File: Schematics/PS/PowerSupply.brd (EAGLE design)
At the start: 99.1 x 76.2 mm, 38 parts, among them T1 IRFP240, T2 IRFP240

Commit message: PS schem updates
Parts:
- added C10, C7, C8, C9: 0.1uF, rcl:C102-064X133
- added C11, C12: 1uF, rcl:C102-064X133
- added C13, C19: 15,000uF, Amplifier_Parts:PHI-35
- added D10, D5, D8, D9: VS-ETL1506-M3, Amplifier_Parts:VS-ETL1506-M3
- added R12: 100, resistor:0207/15
- added R16: 2k, rcl:VTA52
- added R17, R18: 1, rcl:0411/12
- R2: value 100 -> 2k; device resistor:0207/15 -> rcl:VTA52
- R6: value 560 -> 330
- R7: value 390 -> 33; device rcl:0204V -> rcl:0309V
- moved R2 358.2 mm to (-114.0, -270.5), turned to 0 degrees
- moved R7 282.3 mm to (-127.5, -186.2), turned to 0 degrees
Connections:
- net N$24 renamed VAC+40
- net N$26 renamed VAC+15
- net N$27 renamed VAC-15
- net N$9 renamed VAC-40
- removed net N$25: TRAFO1.P$13
- removed net N$28: TRAFO1.P$18
- new net N$23: D5.P$4, D8.P$3
- new net N$24: D10.C, D9.A
- new net N$8: C9.2, R17.2
- new net N$9: D5.A, D8.C
- new net SGND: C10.1, C11.2, C12.1, C13.+, C19.-, C7.2, C8.1, R12.1, R16.2, R17.1, R2.1, TRAFO1.P$13, TRAFO1.P$18
- new net VEE: C12.2, C13.-, C8.2, D10.A, D8.A, R16.1, R18.1
- net GND: now also R12.2; no longer R2.1
- net N$10: now also R7.1; no longer R7.2
- net N$11: now also R7.2; no longer R7.1
- net N$3: now also C10.2, R18.2; no longer R2.2, U$3.P$3
- net VCC: now also C11.1, C19.+, C7.1, C9.1, D5.C, D9.C, R2.2
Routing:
- net N$10: track 36.1 -> 9.41 mm
- net N$3: track 12.4 -> 0.00 mm
- net N$11: track 23.7 -> 17.3 mm

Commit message: updates to PS
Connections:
- removed net N$24: D10.C, D9.A
- removed net N$9: D5.A, D8.C
- net VAC+40: now also D5.A, D8.C
- net VAC-40: now also D10.C, D9.A
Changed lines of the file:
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@@
 <contactref element="TRAFO1" pad="P$11"/>
 <contactref element="TRAFO1" pad="P$12"/>
+<contactref element="D5" pad="A"/>
+<contactref element="D8" pad="C"/>
 <wire x1="-120.904" y1="-124.206" x2="-125.984" y2="-124.206" width="0" layer="19" extent="1-1"/>
+<wire x1="-135.684" y1="-290.068" x2="-125.984" y2="-124.206" width="0" layer="19" extent="1-1"/>
+<wire x1="-158.194" y1="-290.068" x2="-135.684" y2="-290.068" width="0" layer="19" extent="1-1"/>
 </signal>
 <signal name="VAC-40">
 <contactref element="TRAFO1" pad="P$14"/>
 <contactref element="TRAFO1" pad="P$15"/>
+<contactref element="D9" pad="A"/>
+<contactref element="D10" pad="C"/>
 <wire x1="-105.664" y1="-124.206" x2="-110.744" y2="-124.206" width="0" layer="19" extent="1-1"/>
+<wire x1="-168.704" y1="-290.068" x2="-110.744" y2="-124.206" width="0" layer="19" extent="1-1"/>
+<wire x1="-191.214" y1="-290.068" x2="-168.704" y2="-290.068" width="0" layer="19" extent="1-1"/>
 </signal>
 <signal name="VAC+15">
@@
 <wire x1="-129.286" y1="-270.51" x2="-118.618" y2="-280.416" width="0" layer="19" extent="1-1"/>
 </signal>
-<signal name="N$9">
-<contactref element="D5" pad="A"/>
-<contactref element="D8" pad="C"/>
-<wire x1="-135.684" y1="-290.068" x2="-158.194" y2="-290.068" width="0" layer="19" extent="1-1"/>
-</signal>
-<signal name="N$24">
-<contactref element="D9" pad="A"/>
-<contactref element="D10" pad="C"/>
-<wire x1="-168.704" y1="-290.068" x2="-191.214" y2="-290.068" width="0" layer="19" extent="1-1"/>
-</signal>
 </signals>

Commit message: updates to PS schematic, created special 1N4004 part
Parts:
- added C14, C21, C22: 1uF, rcl:E2,5-6
- added C18, C20: 0.1uF, rcl:C102-064X133
- added C6: 10uF, rcl:C102-064X133
- added D11, D12, D13, D14, D15, D16: 1N4004, Amplifier_Parts:1N4004
- added IC1: LM317MABDT, v-reg:DPACK
- added R19, R20: 10k, rcl:0204V
- D1: device diode:DO41-10 -> Amplifier_Parts:1N4004
- moved TRAFO1 187.3 mm to (28.4, 49.8)
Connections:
- net N$12 renamed MUTE
- removed net N$3: C10.2, R18.2
- new net N$25: C10.1, R18.1
- new net N$26: C6.1, D12.A, IC1.1, R19.1, R20.2
- new net VCC1: C18.1, C21.+, D11.C, D13.C, D15.C, IC1.3
- new net VEE1: C20.2, C22.-, D14.A, D16.A
- net N$23: now also C14.+, D11.A, D12.C, IC1.4, R19.2; no longer D5.P$4, D8.P$3
- net SGND: now also C14.-, C18.2, C20.1, C21.-, C22.+, C6.2, R18.2, R20.1; no longer C10.1
- net VAC+15: now also D13.A, D14.C
- net VAC-15: now also D15.A, D16.C
- net VAC-40: now also D10.P$4
- net VCC: no longer U$3.P$2
- net VEE: now also C10.2; no longer R18.1
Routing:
- net N$10: track 9.41 -> 15.1 mm

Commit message: updates to PS, it is finished
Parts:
- added C16, C23, C25: 1uF, rcl:E2,5-6
- added C24: 10uF, resistor:C025-025X050
- added D17, D18: 1N4004, Amplifier_Parts:1N4004
- added IC2: LM337, Amplifier_Parts:LM337
- added R21, R22: 10k, rcl:0204V
- C1: device rcl:C050-035X075 -> resistor:C025-025X050
- C6: device rcl:C102-064X133 -> resistor:C025-025X050
- D6, D7: value 1N4933 -> 1N4004; device diode:DO41-10 -> Amplifier_Parts:1N4004
- U$3: value SCREW_TERMINAL_5 -> SCREW_TERMINAL_6; device Amplifier_Parts:SCREW_TERMINAL_5 -> Amplifier_Parts:SCREW_TERMINAL_6
- moved D6 362.0 mm to (-223.5, -449.6)
- moved D7 358.5 mm to (-225.0, -451.9)
- moved C14 128.6 mm to (-223.0, -456.2)
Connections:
- removed net N$23: C14.+, D11.A, D12.C, IC1.4, R19.2
- removed net VCC1: C18.1, C21.+, D11.C, D13.C, D15.C, IC1.3
- removed net VEE1: C20.2, C22.-, D14.A, D16.A
- new net N$3: C24.2, D17.C, IC2.1, R21.1, R22.2
- new net V-: C25.-
- new net V-15UN: C20.2, C22.-, C23.-, D14.A, D16.A, D18.A, IC2.4
- new net V15+: C14.+, D11.A, D12.C, IC1.4, R19.2, U$3.P$2
- new net V15-: D17.A, D18.C, IC2.3, R22.1, U$3.P$4
- new net V15UN: C16.+, C18.1, C21.+, D11.C, D13.C, D15.C, IC1.3
- net GND: now also U$2.P$5
- net MUTE: now also U$3.P$6
- net PE: no longer U$2.P$5
- net SGND: now also C16.-, C23.+, C24.1, C25.+, R21.2, U$3.P$3
- net VCC: now also U$3.P$1
- net VEE: now also U$3.P$5

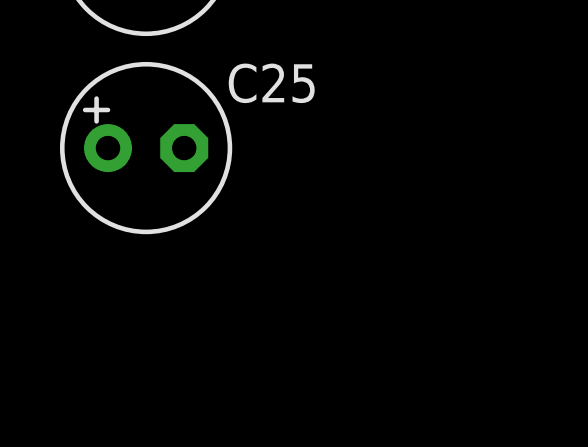
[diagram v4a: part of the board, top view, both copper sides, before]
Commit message: added DC blocking cap on trafo
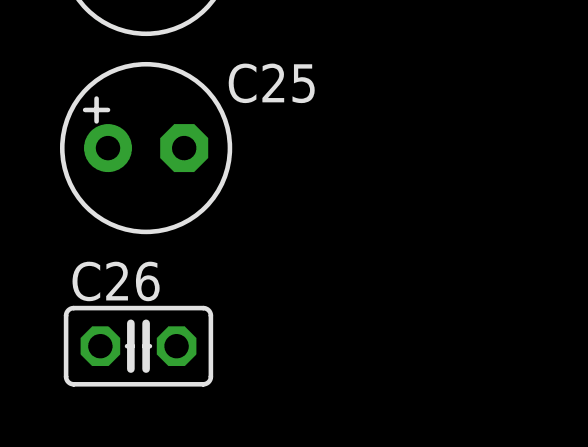
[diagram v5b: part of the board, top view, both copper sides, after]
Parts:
- added C26: 1uF, resistor:C025-025X050
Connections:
- new net N$9: C26.2, TRAFO1.P$10, TRAFO1.P$6, TRAFO1.P$7, TRAFO1.P$8, TRAFO1.P$9
- net GND: now also C26.1; no longer TRAFO1.P$10, TRAFO1.P$6, TRAFO1.P$7, TRAFO1.P$8, TRAFO1.P$9
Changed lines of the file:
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@@
 <element name="C14" library="rcl" package="E2,5-6" value="1uF" x="-223.012" y="-456.184"/>
 <element name="C25" library="rcl" package="E2,5-6" value="1uF" x="-223.012" y="-462.788"/>
+<element name="C26" library="resistor" package="C025-025X050" value="1uF" x="-223.266" y="-469.392"/>
 </elements>
 <signals>
@@
 <contactref element="U$1" pad="COIL+"/>
 <contactref element="U$6" pad="V-"/>
-<contactref element="TRAFO1" pad="P$7"/>
-<contactref element="TRAFO1" pad="P$6"/>
-<contactref element="TRAFO1" pad="P$8"/>
-<contactref element="TRAFO1" pad="P$9"/>
-<contactref element="TRAFO1" pad="P$10"/>
 <contactref element="U$5" pad="4"/>
 <contactref element="C1" pad="1"/>
@@
 <contactref element="R12" pad="2"/>
 <contactref element="U$2" pad="P$5"/>
-<wire x1="-117.602" y1="-141.224" x2="-61.976" y2="-105.791" width="0" layer="19" extent="1-1"/>
-<wire x1="-127.254" y1="-153.416" x2="-117.602" y2="-141.224" width="0" layer="19" extent="1-1"/>
-<wire x1="-127.254" y1="-159.766" x2="-127.254" y2="-153.416" width="0" layer="19" extent="1-1"/>
-<wire x1="-114.046" y1="-192.024" x2="-127.254" y2="-159.766" width="0" layer="19" extent="1-1"/>
+<contactref element="C26" pad="1"/>
+<wire x1="-114.046" y1="-192.024" x2="-224.536" y2="-469.392" width="0" layer="19" extent="1-1"/>
+<wire x1="-127.254" y1="-159.766" x2="-114.046" y2="-192.024" width="0" layer="19" extent="1-1"/>
+<wire x1="-127.254" y1="-153.416" x2="-127.254" y2="-159.766" width="0" layer="19" extent="1-1"/>
+<wire x1="-117.602" y1="-141.224" x2="-127.254" y2="-153.416" width="0" layer="19" extent="1-1"/>
+<wire x1="-61.976" y1="-105.791" x2="-117.602" y2="-141.224" width="0" layer="19" extent="1-1"/>
 <wire x1="1.864" y1="-71.572" x2="-61.976" y2="-105.791" width="0" layer="19" extent="1-1"/>
 <wire x1="1.524" y1="-40.64" x2="1.864" y2="-71.572" width="0" layer="19" extent="1-1"/>
+<wire x1="10.668" y1="-35.306" x2="1.524" y2="-40.64" width="0" layer="19" extent="1-1"/>
 <wire x1="-9.286" y1="-42.578" x2="1.524" y2="-40.64" width="0" layer="19" extent="1-1"/>
-<wire x1="10.668" y1="-35.306" x2="1.524" y2="-40.64" width="0" layer="19" extent="1-1"/>
 <wire x1="30.48" y1="7.62" x2="10.668" y2="-35.306" width="0" layer="19" extent="16-16"/>
-<wire x1="30.988" y1="49.784" x2="25.287265625" y2="52.367478125" width="0" layer="19" extent="1-1"/>
-<wire x1="36.068" y1="49.784" x2="30.988" y2="49.784" width="0" layer="19" extent="1-1"/>
-<wire x1="41.148" y1="49.784" x2="36.068" y2="49.784" width="0" layer="19" extent="1-1"/>
-<wire x1="46.228" y1="49.784" x2="41.148" y2="49.784" width="0" layer="19" extent="1-1"/>
-<wire x1="51.308" y1="49.784" x2="46.228" y2="49.784" width="0" layer="19" extent="1-1"/>
-<wire x1="55.55415" y1="45.591403125" x2="51.308" y2="49.784" width="0" layer="19" extent="1-1"/>
-<wire x1="45.658725" y1="43.20528125" x2="46.228" y2="49.784" width="0" layer="19" extent="1-1"/>
+<wire x1="4.54" y1="29.16" x2="8.298521875" y2="37.41" width="0" layer="19" extent="16-16"/>
+<wire x1="44.892303125" y1="30.808921875" x2="48.702303125" y2="18.108921875" width="0" layer="19" extent="1-1"/>
+<wire x1="45.658725" y1="43.20528125" x2="44.892303125" y2="30.808921875" width="0" layer="19" extent="1-1"/>
+<wire x1="55.55415" y1="45.591403125" x2="45.658725" y2="43.20528125" width="0" layer="19" extent="1-1"/>
 <wire x1="59.567503125" y1="39.844834375" x2="55.55415" y2="45.591403125" width="0" layer="19" extent="1-1"/>
-<wire x1="4.54" y1="29.16" x2="8.298521875" y2="37.41" width="0" layer="19" extent="16-16"/>
 <wire x1="70.620678125" y1="34.528765625" x2="59.567503125" y2="39.844834375" width="0" layer="19" extent="1-1"/>
-<wire x1="44.892303125" y1="30.808921875" x2="45.658725" y2="43.20528125" width="0" layer="19" extent="1-1"/>
 <wire x1="56.795371875" y1="3.327840625" x2="48.37338125" y2="17.78" width="0" layer="19" extent="16-16"/>
 <wire x1="61.9296125" y1="3.109978125" x2="56.795371875" y2="3.327840625" width="0" layer="19" extent="1-1"/>
@@
 <contactref element="C25" pad="-"/>
 </signal>
+<signal name="N$9">
+<contactref element="TRAFO1" pad="P$6"/>
+<contactref element="C26" pad="2"/>
+<contactref element="TRAFO1" pad="P$10"/>
+<contactref element="TRAFO1" pad="P$7"/>
+<contactref element="TRAFO1" pad="P$8"/>
+<contactref element="TRAFO1" pad="P$9"/>
+<wire x1="30.988" y1="49.784" x2="-221.996" y2="-469.392" width="0" layer="19" extent="1-1"/>
+<wire x1="36.068" y1="49.784" x2="30.988" y2="49.784" width="0" layer="19" extent="1-1"/>
+<wire x1="41.148" y1="49.784" x2="36.068" y2="49.784" width="0" layer="19" extent="1-1"/>
+<wire x1="46.228" y1="49.784" x2="41.148" y2="49.784" width="0" layer="19" extent="1-1"/>
+<wire x1="51.308" y1="49.784" x2="46.228" y2="49.784" width="0" layer="19" extent="1-1"/>
+</signal>
 </signals>

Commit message: updates to PS, fixed GND issue
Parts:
- added C28: 1nF, rcl:C102-064X133
- added D19: 1N4004, Amplifier_Parts:1N4004
- C10, C9: value 0.1uF -> 10nF
- C7, C8: value 0.1uF -> 1nF
- moved C14 588.4 mm to (-29.3, 99.4)
- moved C24 588.4 mm to (-21.0, 119.0)
- moved C25 588.4 mm to (-29.3, 92.8)
- moved C26 588.4 mm to (-29.6, 86.2)
- moved D18 588.4 mm to (-28.3, 108.3)
- moved D6 588.4 mm to (-29.8, 106.0)
- moved D7 588.4 mm to (-31.4, 103.8)
- moved C16 494.9 mm to (154.3, -86.5)
- moved C18 494.9 mm to (170.6, -59.1)
- moved C20 494.9 mm to (184.0, -59.1)
- moved C21 494.9 mm to (166.8, -65.4)
- moved C22 494.9 mm to (166.8, -72.0)
- moved C23 494.9 mm to (154.3, -93.1)
- moved D13 494.9 mm to (172.1, -31.1)
- moved D14 494.9 mm to (188.6, -31.1)
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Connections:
- new net N$12: C28.1, U$2.P$5
- net GND: now also C28.2; no longer U$2.P$5
- net N$17: now also D19.A
- net N$6: now also D19.C
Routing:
- net GND: track 140.5 -> 0.00 mm
- net N$18: track 88.0 -> 0.00 mm
- net MUTE: track 86.4 -> 0.00 mm
- net N$11: track 17.3 -> 0.00 mm
- net N$10: track 15.1 -> 0.00 mm
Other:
- board size 99.1 x 76.2 mm -> 152.4 x 127 mm

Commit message: making a commit before i start new schematic
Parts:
- removed C13, C19: 15,000uF, Amplifier_Parts:PHI-35
- removed C3: 1uF, rcl:C102-064X133
- removed L1: CHOKE, Amplifier_Parts:CHOKE
- added L2: CHOKE, Amplifier_Parts:CHOKE
- moved D19 355.0 mm to (93.3, 110.2), turned to 180 degrees
- moved C6 307.6 mm to (200.4, 61.9)
- moved R19 306.4 mm to (197.6, 73.3)
- moved D12 306.3 mm to (211.1, 70.6)
- moved C28 295.6 mm to (19.7, 87.0), turned to 270 degrees
- moved R20 263.7 mm to (178.5, 27.2)
- moved IC1 244.7 mm to (167.8, 42.9)
- moved TRAFO1 237.8 mm to (123.6, 101.1)
- moved T2 224.7 mm to (141.0, 118.4), turned to 270 degrees
- moved C25 217.3 mm to (188.0, 89.9)
- moved C14 214.7 mm to (184.5, 79.7)
- moved R4 205.6 mm to (99.3, 120.9), turned to 270 degrees
- moved R16 203.7 mm to (15.5, 52.4)
- moved C7 203.5 mm to (44.4, 69.2)
- moved C12 203.4 mm to (41.5, 60.2)
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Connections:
- removed net N$16: L1.PASS12, U$2.P$4
- removed net PE: C3.2
- new net EGND: C28.1, U$2.P$3
- new net SOMENET: C17.1, L2.PASS1, R10.1, R11.1, R9.1, U$1.COM
- net GND: now also C4.-; no longer C17.1, L1.PASS22, R10.1, R11.1, R9.1, U$1.COM
- net N$10: no longer C3.1
- net N$12: now also U$4.P$2, U$4.P$4; no longer C28.1
- net N$15: now also L2.PASS12, U$2.P$2; no longer L1.PASS1, U$2.P$6
- net N$2: now also L2.PASS22, U$2.P$4; no longer U$2.P$2, U$4.P$1, U$4.P$3
- net N$4: now also L2.PASS2; no longer L1.PASS2
- net N$5: now also U$2.P$6, U$4.P$1, U$4.P$3; no longer U$2.P$3, U$4.P$2, U$4.P$4
- net SGND: no longer C13.+, C19.-
- net VAC-40: no longer D10.P$4
- net VCC: no longer C19.+
- net VEE: no longer C13.-
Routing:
- net V+: track 0.00 -> 128.5 mm
- net N$22: track 0.00 -> 91.1 mm
- net N$18: track 0.00 -> 75.5 mm
- net SOMENET: track 0.00 -> 55.4 mm
- net SGND: track 0.00 -> 54.5 mm
- net N$20: track 0.00 -> 53.1 mm
- net N$12: track 0.00 -> 48.8 mm
- net N$9: track 0.00 -> 32.1 mm
- net N$17: track 0.00 -> 27.3 mm
- net EGND: track 0.00 -> 27.0 mm
- net N$5: track 0.00 -> 26.3 mm
- net N$6: track 0.00 -> 20.5 mm
- net N$2: track 0.00 -> 19.1 mm
- net N$19: track 0.00 -> 18.1 mm
- net N$15: track 0.00 -> 17.8 mm
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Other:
- board size 152.4 x 127 mm -> 157.5 x 127 mm

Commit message: fixed PS issue
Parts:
- removed C25: 1uF, rcl:E2,5-6
- added C13: 1uF, rcl:C102-064X133
- added C3: 1uF, rcl:E2,5-6
- moved C15 22.7 mm to (44.4, 76.4)
- moved D8 6.64 mm to (87.8, 41.5)
- moved D10 6.22 mm to (106.0, 41.5)
- moved D5 6.01 mm to (71.5, 52.7)
- moved D9 5.62 mm to (125.0, 41.5)
- moved C7 2.17 mm to (43.7, 67.2)
- moved R6 1.71 mm to (91.7, 66.6)
- moved D1 0.78 mm to (90.8, 82.4)
- moved R8 0.65 mm to (82.6, 65.2), turned to 0 degrees
- moved R1 0.63 mm to (82.9, 68.8)
- moved D2 0.48 mm to (87.6, 65.5)
- moved R7 0.48 mm to (93.1, 71.0)
- moved LED2 0.27 mm to (89.6, 85.3)
- moved D3 0.05 mm to (82.4, 72.4), turned to 180 degrees
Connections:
- removed net V-: C25.-
- net GND: now also C13.2
- net N$10: now also C13.1
- net SGND: now also C3.+; no longer C25.+
- net V15-: now also C3.-
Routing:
- net VCC: track 0.00 -> 119.0 mm
- net VAC+40: track 0.00 -> 50.0 mm
- net VEE: track 0.00 -> 45.5 mm
- net VAC-40: track 0.00 -> 34.9 mm
- net N$1: track 0.00 -> 17.4 mm
- net N$10: track 0.00 -> 15.6 mm
- net N$11: track 0.00 -> 7.61 mm
- net MUTE: track 0.00 -> 4.44 mm
- added copper zone on layer 16, net SGND
